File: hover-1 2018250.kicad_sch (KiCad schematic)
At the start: 46 parts, among them Q10 TIP127, Q12 G1, Q14 G1, Q15 G1, Q6 G1, Q9 TIP127, SW1 SW_SPST, U1 GD32F130C8, U5 SOT-223, U6 LM78M05_TO252

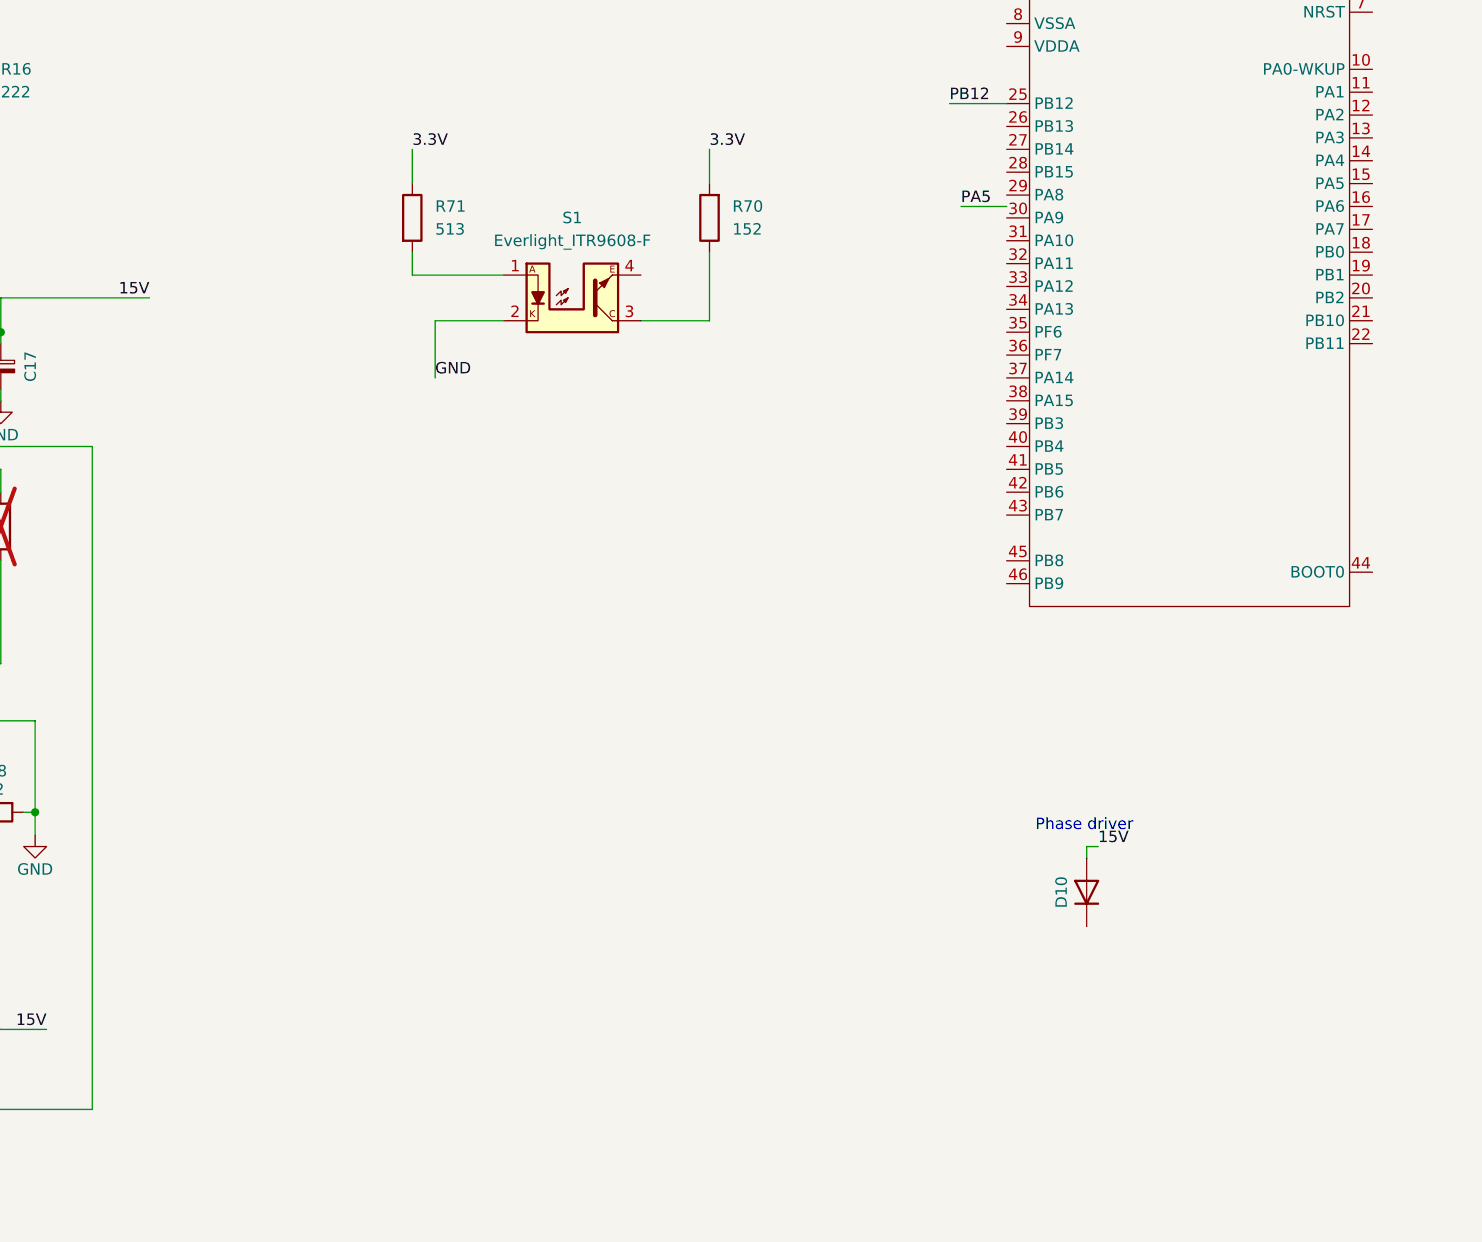
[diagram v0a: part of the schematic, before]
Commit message: Add Left op amp Schematic and traces
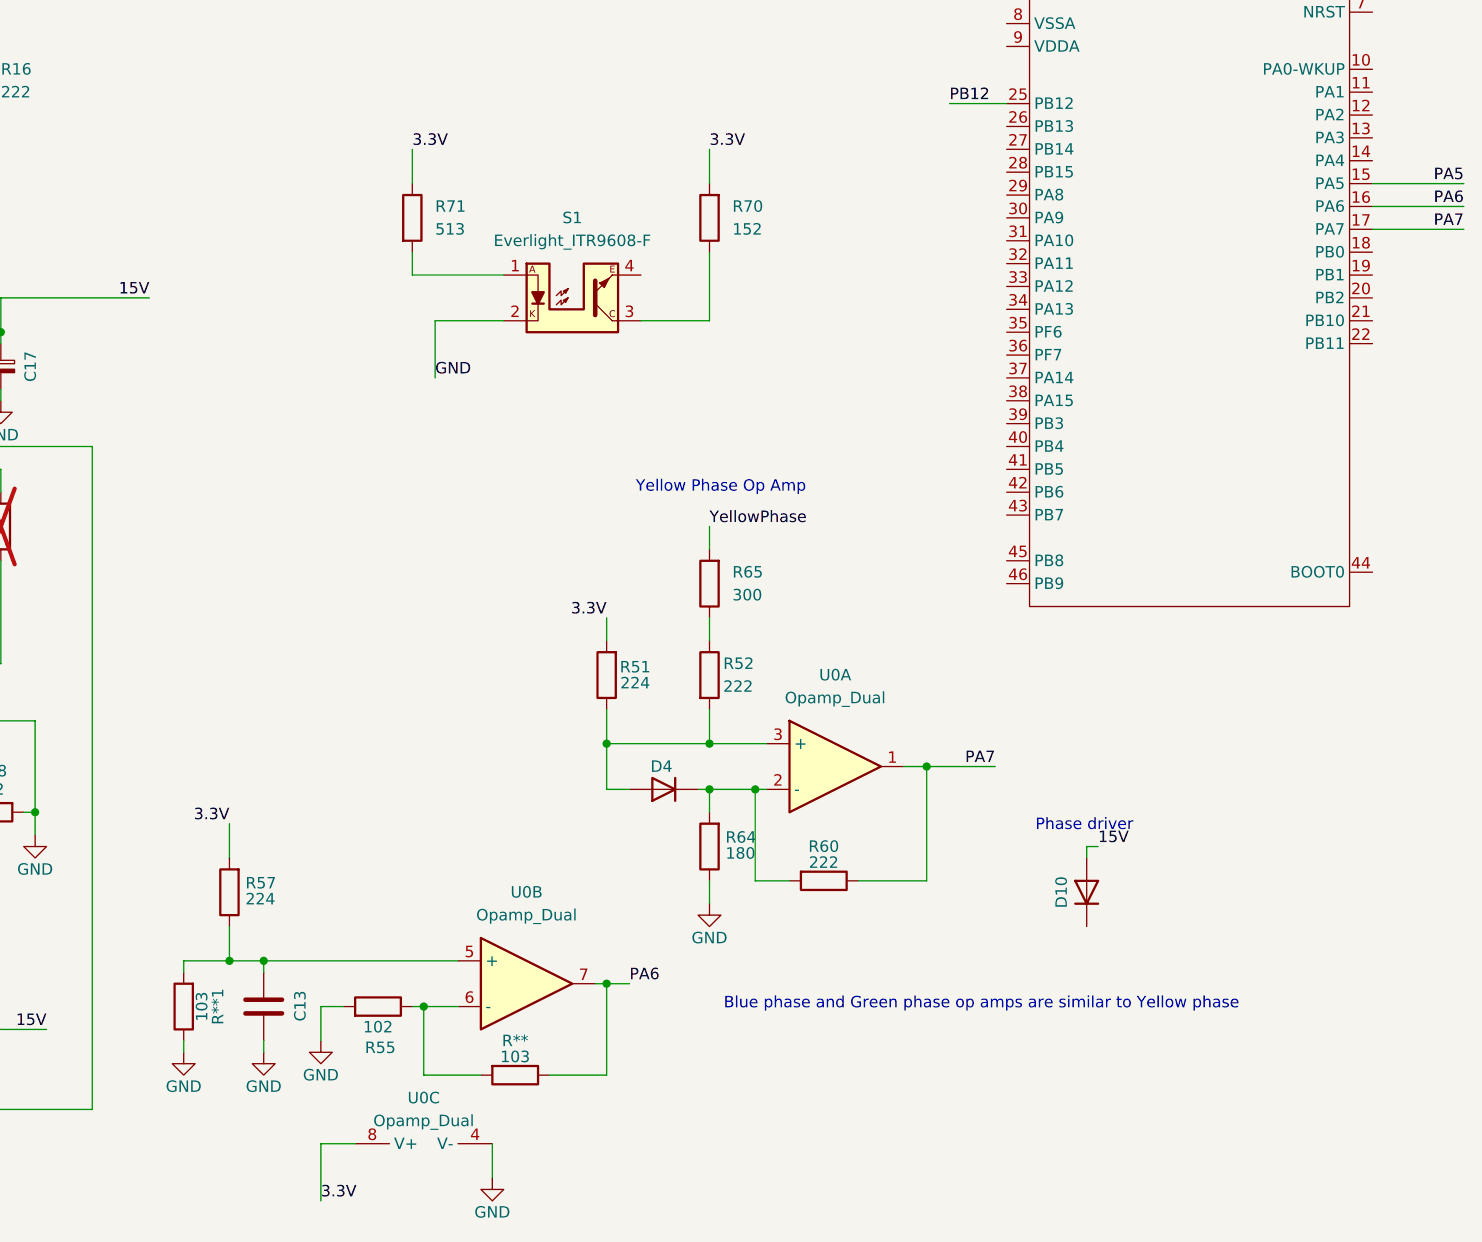
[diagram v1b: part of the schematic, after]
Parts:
- added C13: C_1206_3216Metric_Pad1.33x1.80mm_HandSolder, Capacitor_SMD:C_1206_3216Metric_Pad1.33x1.80mm_HandSolder, symbol Device:C
- added D4: D_SOD-123, Diode_SMD:D_2010_5025Metric, symbol Device:D
- added R**, R**1: 103, Resistor_SMD:R_0603_1608Metric_Pad0.98x0.95mm_HandSolder, symbol Device:R
- added R51, R57: 224, Resistor_SMD:R_0603_1608Metric_Pad0.98x0.95mm_HandSolder, symbol Device:R
- added R52, R60: 222, Resistor_SMD:R_0603_1608Metric_Pad0.98x0.95mm_HandSolder, symbol Device:R
- added R55: 102, Resistor_SMD:R_0603_1608Metric_Pad0.98x0.95mm_HandSolder, symbol Device:R
- added R64: 180, Resistor_SMD:R_0603_1608Metric_Pad0.98x0.95mm_HandSolder, symbol Device:R
- added R65: 300, Resistor_SMD:R_0603_1608Metric_Pad0.98x0.95mm_HandSolder, symbol Device:R
- added U0: Opamp_Dual, symbol Device:Opamp_Dual
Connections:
- net 3.3V: now also R51.2, R57.2, U0.8 (V+)
- net GND: now also C13.1, R**1.1, R55.2, R64.1, U0.4 (V-)
- net PA5: now also U1.15 (PA5)
- net PA6: now reaches U1.16 (PA6)
- net PA6: now also R**.1, U0.7
- net PA7: now reaches U1.17 (PA7)
- net PA7: now also R60.1, U0.1
- new net: R52.1, R65.1
- new net: D4.2 (A), R51.1, R52.2, U0.3 (+)
- new net: C13.2, R**1.2, R57.1, U0.5 (+)
- new net: D4.1 (K), R60.2, R64.2, U0.2 (-)
- new net: R**.2, R55.1, U0.6 (-)
- new net YellowPhase: R65.2
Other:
- note added: "Blue phase and Green phase op amps are similar to Yellow phase"
- note added: "Yellow Phase Op Amp"

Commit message: Organize schematic
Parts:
- removed R16: 222, Resistor_SMD:R_0603_1608Metric_Pad0.98x0.95mm_HandSolder, symbol Device:R
- added R3: 222, Resistor_SMD:R_0603_1608Metric_Pad0.98x0.95mm_HandSolder, symbol Device:R
- C17: value ~ -> CP_Radial_D8.0mm_P3.80mm; symbol Device:C_Polarized_Small -> Device:C_Polarized
- D10: value ~ -> D_2010_5025Metric
- D2: value T4 -> D_2010_5025Metric
- D8: value W6 -> D_Zener; symbol Device:D -> Device:D_Zener
- L1: value ~ -> L_Radial_D8.7mm_P5.00mm_Fastron_07HCP
- Q10, Q9: value TIP127 -> TO-252-2
- Q12, Q14: value G1 -> SOT-323_SC-70
- Q15: value G1 -> SC-59
- R15, R2, R29, R32, R45, R46: now fitted
- R30, R40: value 102 -> 302
- U1: value GD32F130C8 -> LQFP-48_7x7mm_P0.5mm
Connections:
- net 15V: no longer C17.1, L1.1, R28.1, R40.1, U6.1 (VI)
- net 3.3V: now also U1.23 (VSS), U1.47 (VSS); no longer C28.1, R70.2, R71.1, U5.2 (VO)
- net Batt+: no longer Q9.3 (E), R1.2, R9.2
- net GND: now also R15.2; no longer R15.1
- net Power Button: now reaches D2.2 (A), R0.1, SW1.1 (A)
- net Power Button: now also R29.2; no longer R29.1
- net Power Hold: now reaches Q14.1 (B), R2.2
- net Power Hold: now also R15.1, R3.2; no longer R15.2
- net at D6.1 (K), L1.2, Q10.2 (C): now also C11.1; no longer C11.2
- net at C9.1, Q10.1 (B), Q15.3 (C)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: now also R46.2; no longer R46.1
- net at U1.20 (PB2): now also R3.1
- net at Q12.3 (C), Q15.1 (B), R49.1: now also R46.1; no longer R46.2
- net at R49.2: now also C11.2; no longer C11.1
- net 5v renamed +5v
- net PA5: no longer names the net of C20.2, U1.15 (PA5)
- net PA5: now also R29.1; no longer R29.2
- new net +15V: C17.1, L1.1, R28.1, R40.1, U6.1 (VI)
- new net +3.3V: C28.1, R70.2, R71.1, U5.2 (VO)
- new net +Batt: Q9.3 (E), R1.2, R9.2
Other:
- note added: "15V Regulator"
- note added: "3.3V Regulator"
- note added: "5v Regulator"
- note added: "Current Sense?"
- note added: "Motor Phase Current Sense (Yellow)"
- note added: "Power Switch"
- note removed: "3.3V Power"
- note removed: "5v Power"
- note removed: "Yellow Phase Op Amp"
- moved on the sheet: C11, C13, C17, C20, C6, C9, D1, D2, D4, D6, D8, F1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
